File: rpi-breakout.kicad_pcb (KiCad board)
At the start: 2 copper layers, 65 x 30 mm, 31 parts, among them J1 R22, J11 R22, J14 Raspberry_Pi_2_3, J17 Raspberry_Pi_2_3, J18 R22, J19 R22, J3 R22, J5 R22, J7 R22, J9 R22

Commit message: Fix mossing renames from rpi_breakout to rpi-breakout
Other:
- board text added: "github.com/mtrudel/rpi-breakout"
- board text removed: "github.com/mtrudel/rpi_breakout"
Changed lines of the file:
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@@
     (effects (font (size 1.5 1.5) (thickness 0.3)) (justify mirror))
   )
-  (gr_text github.com/mtrudel/rpi_breakout (at 138.037 127.776) (layer B.SilkS)
+  (gr_text github.com/mtrudel/rpi-breakout (at 138.037 127.776) (layer B.SilkS)
     (effects (font (size 1.5 1.5) (thickness 0.3)) (justify mirror))
   )

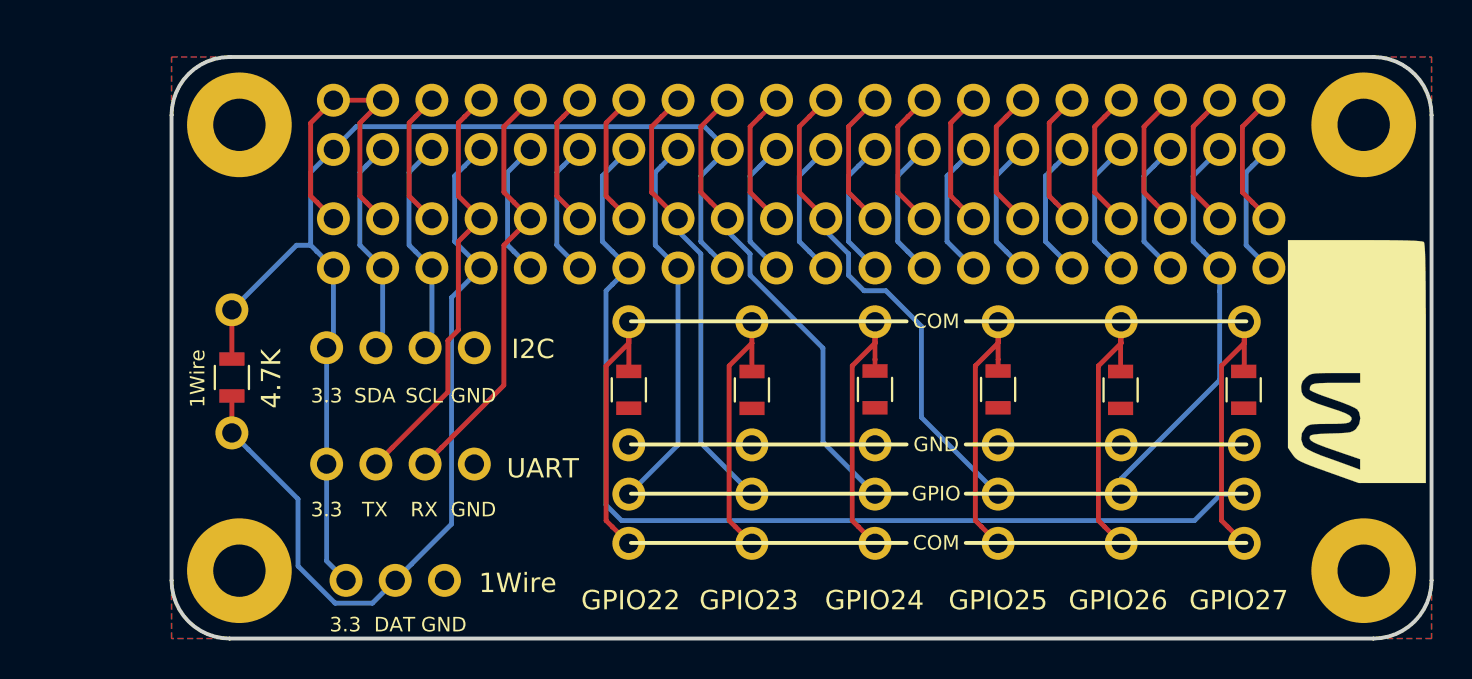
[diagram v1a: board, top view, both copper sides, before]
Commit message: v2.0: Add 2 more GPIOs, re-layout on 100 mil grid
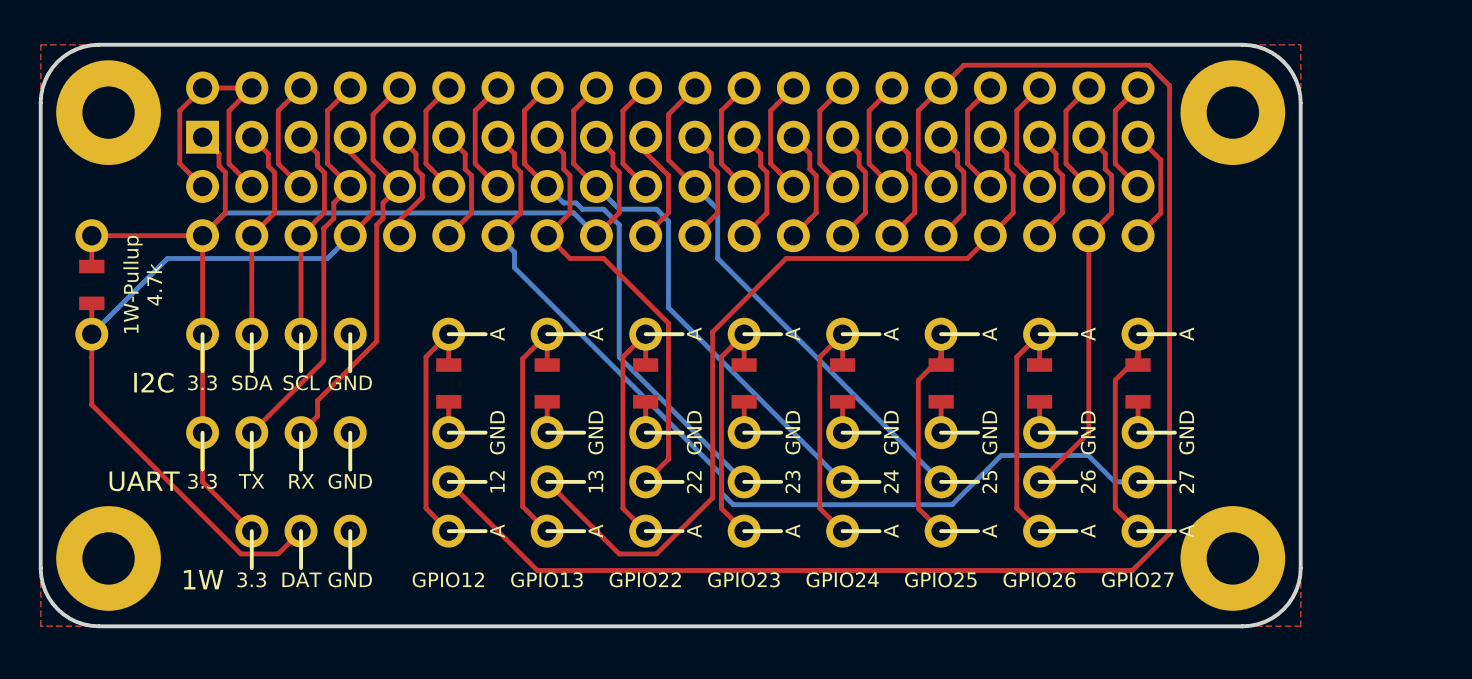
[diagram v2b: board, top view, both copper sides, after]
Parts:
- removed 1Wire: 1Wire, Pin_Headers:Pin_Header_Straight_1x03_Pitch2.54mm
- removed 4.7K: R, Resistors_SMD:R_0805
- removed the I2C at (108.0, 115.0)
- removed the UART at (108.0, 121.0)
- added 1W: 1Wire, moshozenfootprints:Pin_Header_Straight_1x03_Pitch2.54mm, F.Cu at (104.1, 124.5)
- added GPIO12: GPIO12, moshozenfootprints:Pin_Header_Straight_1x03_Pitch2.54mm, F.Cu at (114.3, 119.4)
- added GPIO13: GPIO13, moshozenfootprints:Pin_Header_Straight_1x03_Pitch2.54mm, F.Cu at (119.4, 119.4)
- added I2C: I2C, moshozenfootprints:Pin_Header_Straight_1x04_Pitch2.54mm, F.Cu at (101.6, 114.3)
- added J20: R22, moshozenfootprints:Pin_Header_Straight_1x01_Pitch2.54mm, F.Cu at (119.4, 114.3)
- added J22: R22, moshozenfootprints:Pin_Header_Straight_1x01_Pitch2.54mm, F.Cu at (114.3, 114.3)
- added R7: R, moshozenfootprints:R_0805, F.Cu at (95.9, 111.8)
- added R8: R, moshozenfootprints:R_0805, F.Cu at (119.4, 116.8)
- added R9: R, moshozenfootprints:R_0805, F.Cu at (114.3, 116.8)
- added UART: UART, moshozenfootprints:Pin_Header_Straight_1x04_Pitch2.54mm, F.Cu at (101.6, 119.4)
- G***: moved to B.Cu
- GPIO22, GPIO23, GPIO24, GPIO25, GPIO26, GPIO27: footprint Pin_Headers:Pin_Header_Straight_1x03_Pitch2.54mm -> moshozenfootprints:Pin_Header_Straight_1x03_Pitch2.54mm
- J1, J11, J18, J19, J3, J5, J7, J9: footprint Pin_Headers:Pin_Header_Straight_1x01_Pitch2.54mm -> moshozenfootprints:Pin_Header_Straight_1x01_Pitch2.54mm
- J14, J17: footprint Pin_Headers:Pin_Header_Straight_2x20_Pitch2.54mm -> moshozenfootprints:Pin_Header_Straight_2x20_Pitch2.54mm
- R1, R2, R3, R4, R5, R6: footprint Resistors_SMD:R_0805 -> moshozenfootprints:R_0805
- REF**: moved to F.Cu
- moved G*** 12.1 mm to (150.4, 110.2), turned to 180 degrees
- moved J17 9.54 mm to (101.6, 104.1)
- moved J18 8.84 mm to (95.9, 114.3)
- moved J19 8.18 mm to (95.9, 109.2)
- moved J14 8.08 mm to (101.6, 109.2)
- moved REF** 6.78 mm to (96.8, 125.9)
- moved REF** 6.78 mm to (96.8, 102.9)
- moved REF** 6.78 mm to (154.8, 102.9)
- moved REF** 6.78 mm to (154.8, 125.9)
- moved J11 5.52 mm to (149.9, 114.3)
- moved GPIO27 5.52 mm to (149.9, 119.4)
- moved R6 5.46 mm to (149.9, 116.8)
- moved J5 4.26 mm to (144.8, 114.3)
- moved GPIO26 4.26 mm to (144.8, 119.4)
- moved R3 4.19 mm to (144.8, 116.8)
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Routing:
- net 32: track 7.09 -> 81.7 mm
- net 33: track 7.25 -> 42.3 mm
- net Net-(J20-Pad1): track 0.00 -> 12.8 mm
- net Net-(J22-Pad1): track 0.00 -> 12.7 mm
- net 13: track 53.8 -> 47.5 mm
- net GND: track 57.4 -> 61.1 mm
- net 16: track 23.0 -> 26.5 mm
- net 3.3V: track 60.3 -> 57.0 mm
- net 18: track 24.6 -> 27.7 mm
- net 15: track 19.8 -> 22.8 mm
- net Net-(J5-Pad1): track 15.0 -> 12.7 mm
- net Net-(J11-Pad1): track 15.0 -> 12.7 mm
- net Net-(J1-Pad1): track 15.0 -> 12.7 mm
- net Net-(J10-Pad3): track 14.9 -> 12.7 mm
- net Net-(J3-Pad1): track 14.9 -> 12.7 mm
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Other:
- board text added: "12"
- board text added: "13"
- board text added: "1W-Pullup 4.7k"
- board text added: "22"
- board text added: "23"
- board text added: "24"
- board text added: "25"
- board text added: "26"
- board text added: "27"
- board text added: "A"
- board text added: "v2.0"
- board text removed: "1Wire"
- board text removed: "COM"
- board text removed: "GPIO"
- board text removed: "v1.1"

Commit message: Second pass at v2.0 (previous was unshipped)
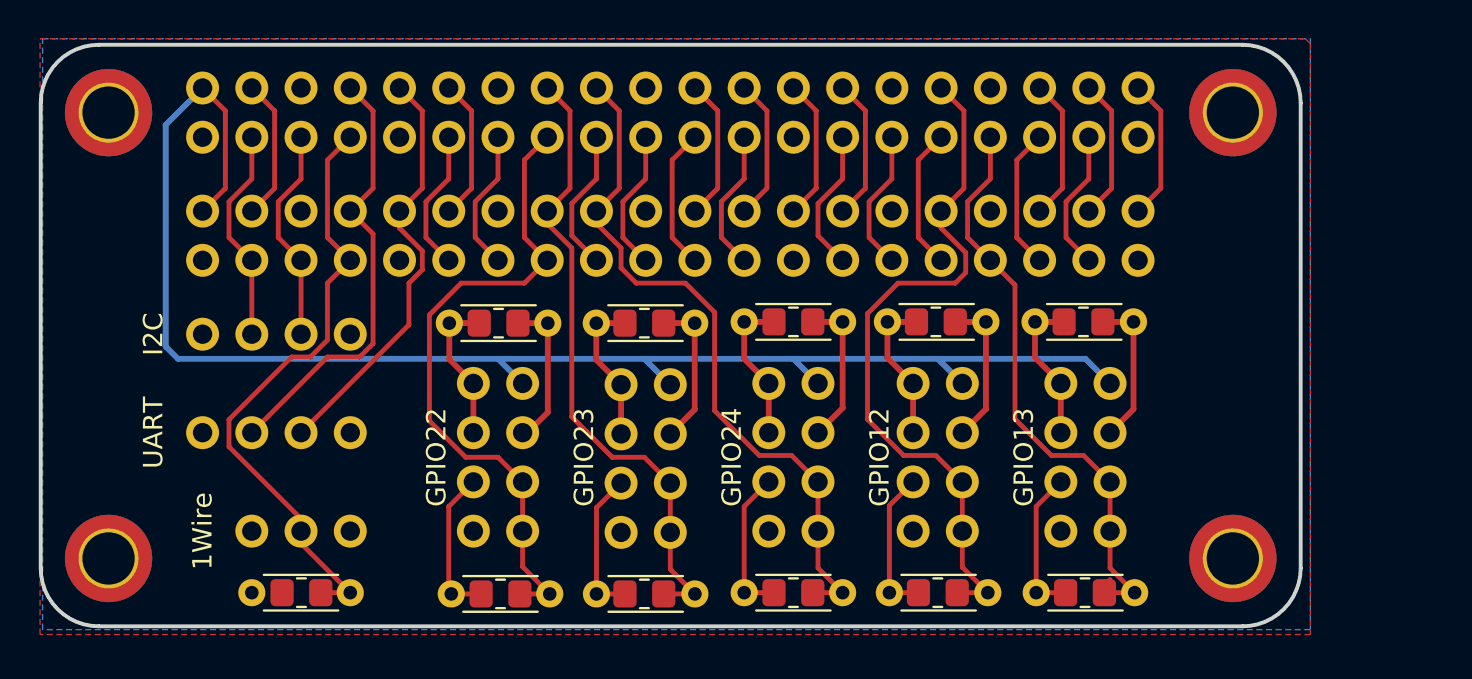
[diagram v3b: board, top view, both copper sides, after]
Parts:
- removed the G*** at (150.4, 110.2)
- removed GPIO25: GPIO25, moshozenfootprints:Pin_Header_Straight_1x03_Pitch2.54mm
- removed GPIO26: GPIO26, moshozenfootprints:Pin_Header_Straight_1x03_Pitch2.54mm
- removed GPIO27: GPIO27, moshozenfootprints:Pin_Header_Straight_1x03_Pitch2.54mm
- removed J1, J11, J18, J19, J20, J22, J3, J5, J7, J9: R22, moshozenfootprints:Pin_Header_Straight_1x01_Pitch2.54mm
- removed R1, R2, R3, R4, R5, R6: R, moshozenfootprints:R_0805
- removed the REF** at (96.8, 125.9)
- removed the REF** at (96.8, 102.9)
- removed the REF** at (154.8, 102.9)
- removed the REF** at (154.8, 125.9)
- added G***: LOGO, Moshozen:Moshozen, B.Cu at (97.2, 114.3)
- added R10: R, Resistor_SMD:R_0805_2012Metric_Pad1.20x1.40mm_HandSolder, F.Cu at (147.0, 113.7)
- added R11: R, Resistor_THT:R_Axial_DIN0204_L3.6mm_D1.6mm_P5.08mm_Horizontal, F.Cu at (149.6, 113.7)
- added R12: R, Resistor_THT:R_Axial_DIN0204_L3.6mm_D1.6mm_P5.08mm_Horizontal, F.Cu at (149.7, 127.6)
- added R13: R, Resistor_THT:R_Axial_DIN0204_L3.6mm_D1.6mm_P5.08mm_Horizontal, F.Cu at (127.0, 113.7)
- added R14: R, Resistor_SMD:R_0805_2012Metric_Pad1.20x1.40mm_HandSolder, F.Cu at (124.4, 113.7)
- added R15: R, Resistor_SMD:R_0805_2012Metric_Pad1.20x1.40mm_HandSolder, F.Cu at (124.4, 127.7)
- added R16: R, Resistor_THT:R_Axial_DIN0204_L3.6mm_D1.6mm_P5.08mm_Horizontal, F.Cu at (127.0, 127.7)
- added R17: R, Resistor_THT:R_Axial_DIN0204_L3.6mm_D1.6mm_P5.08mm_Horizontal, F.Cu at (119.4, 113.7)
- added R18: R, Resistor_SMD:R_0805_2012Metric_Pad1.20x1.40mm_HandSolder, F.Cu at (116.9, 113.7)
- added R19: R, Resistor_SMD:R_0805_2012Metric_Pad1.20x1.40mm_HandSolder, F.Cu at (117.0, 127.7)
- added R20: R, Resistor_THT:R_Axial_DIN0204_L3.6mm_D1.6mm_P5.08mm_Horizontal, F.Cu at (119.5, 127.7)
- added R21: R, Resistor_THT:R_Axial_DIN0204_L3.6mm_D1.6mm_P5.08mm_Horizontal, F.Cu at (142.0, 113.7)
- added R22: R, Resistor_SMD:R_0805_2012Metric_Pad1.20x1.40mm_HandSolder, F.Cu at (139.4, 113.7)
- added R23: R, Resistor_SMD:R_0805_2012Metric_Pad1.20x1.40mm_HandSolder, F.Cu at (139.5, 127.6)
- added R24: R, Resistor_THT:R_Axial_DIN0204_L3.6mm_D1.6mm_P5.08mm_Horizontal, F.Cu at (142.1, 127.6)
- added R25: R, Resistor_THT:R_Axial_DIN0204_L3.6mm_D1.6mm_P5.08mm_Horizontal, F.Cu at (134.6, 113.7)
- added R26: R, Resistor_SMD:R_0805_2012Metric_Pad1.20x1.40mm_HandSolder, F.Cu at (132.1, 113.7)
- added R27: R, Resistor_SMD:R_0805_2012Metric_Pad1.20x1.40mm_HandSolder, F.Cu at (132.1, 127.6)
- added R28: R, Resistor_THT:R_Axial_DIN0204_L3.6mm_D1.6mm_P5.08mm_Horizontal, F.Cu at (134.6, 127.6)
- added REF**: MountingHole_2.7mm_M2.5_ISO7380_Pad_TopBottom, MountingHole:MountingHole_2.7mm_M2.5_ISO7380_Pad_TopBottom, F.Cu at (96.8, 125.9)
- added REF**: MountingHole_2.7mm_M2.5_ISO7380_Pad_TopBottom, MountingHole:MountingHole_2.7mm_M2.5_ISO7380_Pad_TopBottom, F.Cu at (154.8, 125.9)
- added REF**: MountingHole_2.7mm_M2.5_ISO7380_Pad_TopBottom, MountingHole:MountingHole_2.7mm_M2.5_ISO7380_Pad_TopBottom, F.Cu at (154.8, 102.9)
- added REF**: MountingHole_2.7mm_M2.5_ISO7380_Pad_TopBottom, MountingHole:MountingHole_2.7mm_M2.5_ISO7380_Pad_TopBottom, F.Cu at (96.8, 102.9)
- GPIO12, GPIO13, GPIO22, GPIO23, GPIO24: footprint moshozenfootprints:Pin_Header_Straight_1x03_Pitch2.54mm -> Connector_PinHeader_2.54mm:PinHeader_2x04_P2.54mm_Vertical
- J13: renamed from UART; footprint moshozenfootprints:Pin_Header_Straight_1x04_Pitch2.54mm -> Connector_PinHeader_2.54mm:PinHeader_1x04_P2.54mm_Vertical
- J14, J17: footprint moshozenfootprints:Pin_Header_Straight_2x20_Pitch2.54mm -> Connector_PinHeader_2.54mm:PinHeader_2x20_P2.54mm_Vertical
- J15: renamed from I2C; footprint moshozenfootprints:Pin_Header_Straight_1x04_Pitch2.54mm -> Connector_PinHeader_2.54mm:PinHeader_1x04_P2.54mm_Vertical
- J16: renamed from 1W; footprint moshozenfootprints:Pin_Header_Straight_1x03_Pitch2.54mm -> Connector_PinHeader_2.54mm:PinHeader_1x03_P2.54mm_Vertical
- R7, R9: footprint moshozenfootprints:R_0805 -> Resistor_SMD:R_0805_2012Metric_Pad1.20x1.40mm_HandSolder
- R8: footprint moshozenfootprints:R_0805 -> Resistor_THT:R_Axial_DIN0204_L3.6mm_D1.6mm_P5.08mm_Horizontal
- moved R9 34.6 mm to (147.1, 127.6), turned to 180 degrees
- moved GPIO13 26.6 mm to (145.9, 116.8)
- moved GPIO12 24.1 mm to (138.3, 116.8)
- moved R7 19.2 mm to (106.7, 127.6), turned to 0 degrees
- moved R8 18.7 mm to (104.1, 127.6), turned to 0 degrees
- moved GPIO22 9.25 mm to (115.6, 116.8)
- moved GPIO23 6.82 mm to (123.2, 116.9)
- moved GPIO24 4.58 mm to (130.8, 116.8)
- moved J14 1.27 mm to (101.6, 110.5)
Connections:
- GPIO12 pad 1: GND -> Net-(GPIO12-Pin_1)
- GPIO12 pad 2: 32 -> 5V
- GPIO12 pad 3: Net-(J22-Pad1) -> Net-(GPIO12-Pin_1)
- GPIO13 pad 1: GND -> Net-(GPIO13-Pin_1)
- GPIO13 pad 2: 33 -> 5V
- GPIO13 pad 3: Net-(J20-Pad1) -> Net-(GPIO13-Pin_1)
- GPIO22 pad 1: GND -> Net-(GPIO22-Pin_1)
- GPIO22 pad 2: 15 -> 5V
- GPIO22 pad 3: Net-(J1-Pad1) -> Net-(GPIO22-Pin_1)
- GPIO23 pad 1: GND -> Net-(GPIO23-Pin_1)
- GPIO23 pad 2: 16 -> 5V
- GPIO23 pad 3: Net-(J7-Pad1) -> Net-(GPIO23-Pin_1)
- GPIO24 pad 1: GND -> Net-(GPIO24-Pin_1)
- GPIO24 pad 2: 18 -> 5V
- GPIO24 pad 3: Net-(J3-Pad1) -> Net-(GPIO24-Pin_1)
- R8 pad 1: Net-(J20-Pad1) -> 3.3V
- R8 pad 2: GND -> 7
- R9 pad 1: Net-(J22-Pad1) -> 33
- R9 pad 2: GND -> Net-(GPIO13-Pin_5)
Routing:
- net 5V: track 14.6 -> 85.6 mm
- net GND: track 61.1 -> 0.00 mm
- net 3.3V: track 57.0 -> 7.40 mm
- net 32: track 81.7 -> 36.5 mm
- net 13: track 47.5 -> 7.32 mm
- net 22: track 26.7 -> 7.32 mm
- net Net-(J20-Pad1): track 12.8 -> 0.00 mm
- net Net-(J11-Pad1): track 12.7 -> 0.00 mm
- net Net-(J5-Pad1): track 12.7 -> 0.00 mm
- net Net-(J3-Pad1): track 12.7 -> 0.00 mm
- net Net-(J22-Pad1): track 12.7 -> 0.00 mm
- net Net-(J1-Pad1): track 12.7 -> 0.00 mm
- net Net-(J10-Pad3): track 12.7 -> 0.00 mm
- net Net-(J7-Pad1): track 12.7 -> 0.00 mm
- net 37: track 19.8 -> 7.32 mm
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- added copper zone on F.Cu, net 3.3V
- removed copper zone on F.Cu, net GND
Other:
- net class Default removed
- board text removed: "12"
- board text removed: "13"
- board text removed: "1W-Pullup 4.7k"
- board text removed: "22"
- board text removed: "23"
- board text removed: "24"
- board text removed: "25"
- board text removed: "26"
- board text removed: "27"
- board text removed: "3.3"
- board text removed: "A"
- board text removed: "DAT"
- board text removed: "GND"
- board text removed: "RX"
- board text removed: "SCL"
- board text removed: "SDA"
- board text removed: "TX"
